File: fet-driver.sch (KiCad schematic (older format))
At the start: 32 parts, among them Q13 AO3401, Q22 AO3401, Q23 AO3401, Q24 AO3401, Q25 AO3401, Q26 AO3401, Q27 AO3401, Q28 AO3401

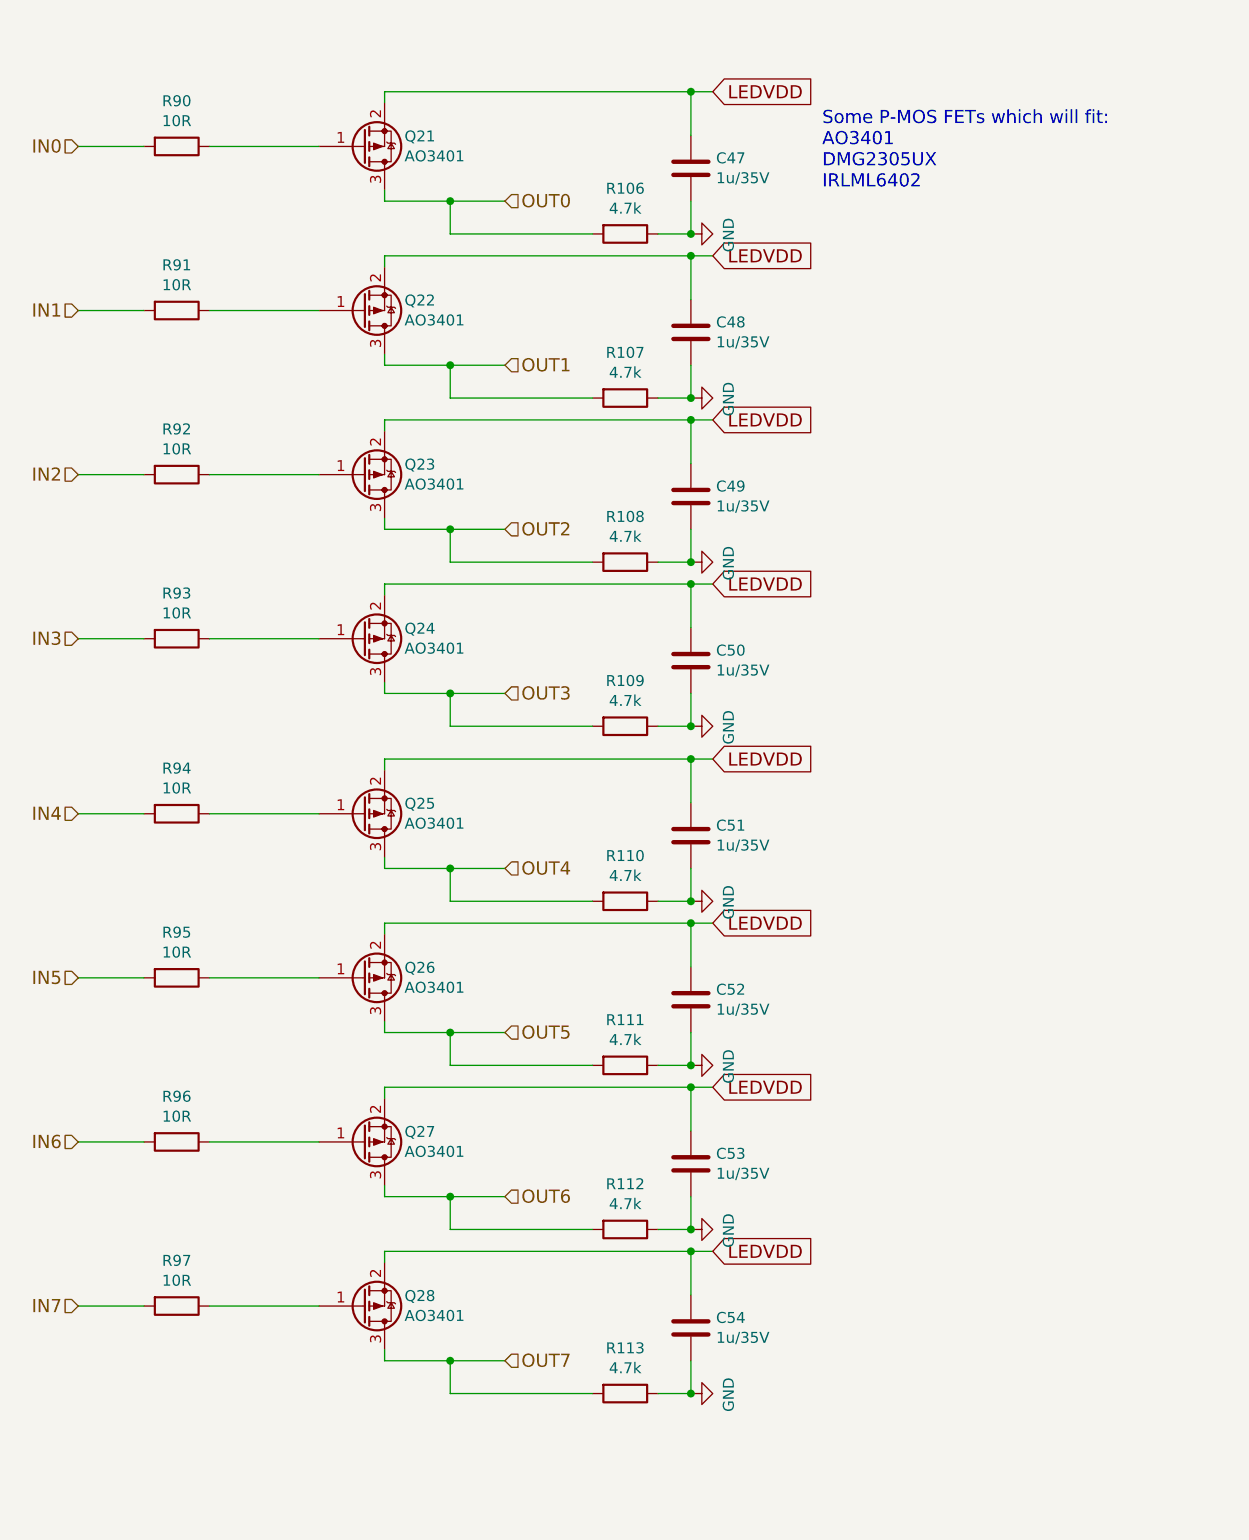
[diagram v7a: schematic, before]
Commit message: Schematics format change due to KiCAD's verup
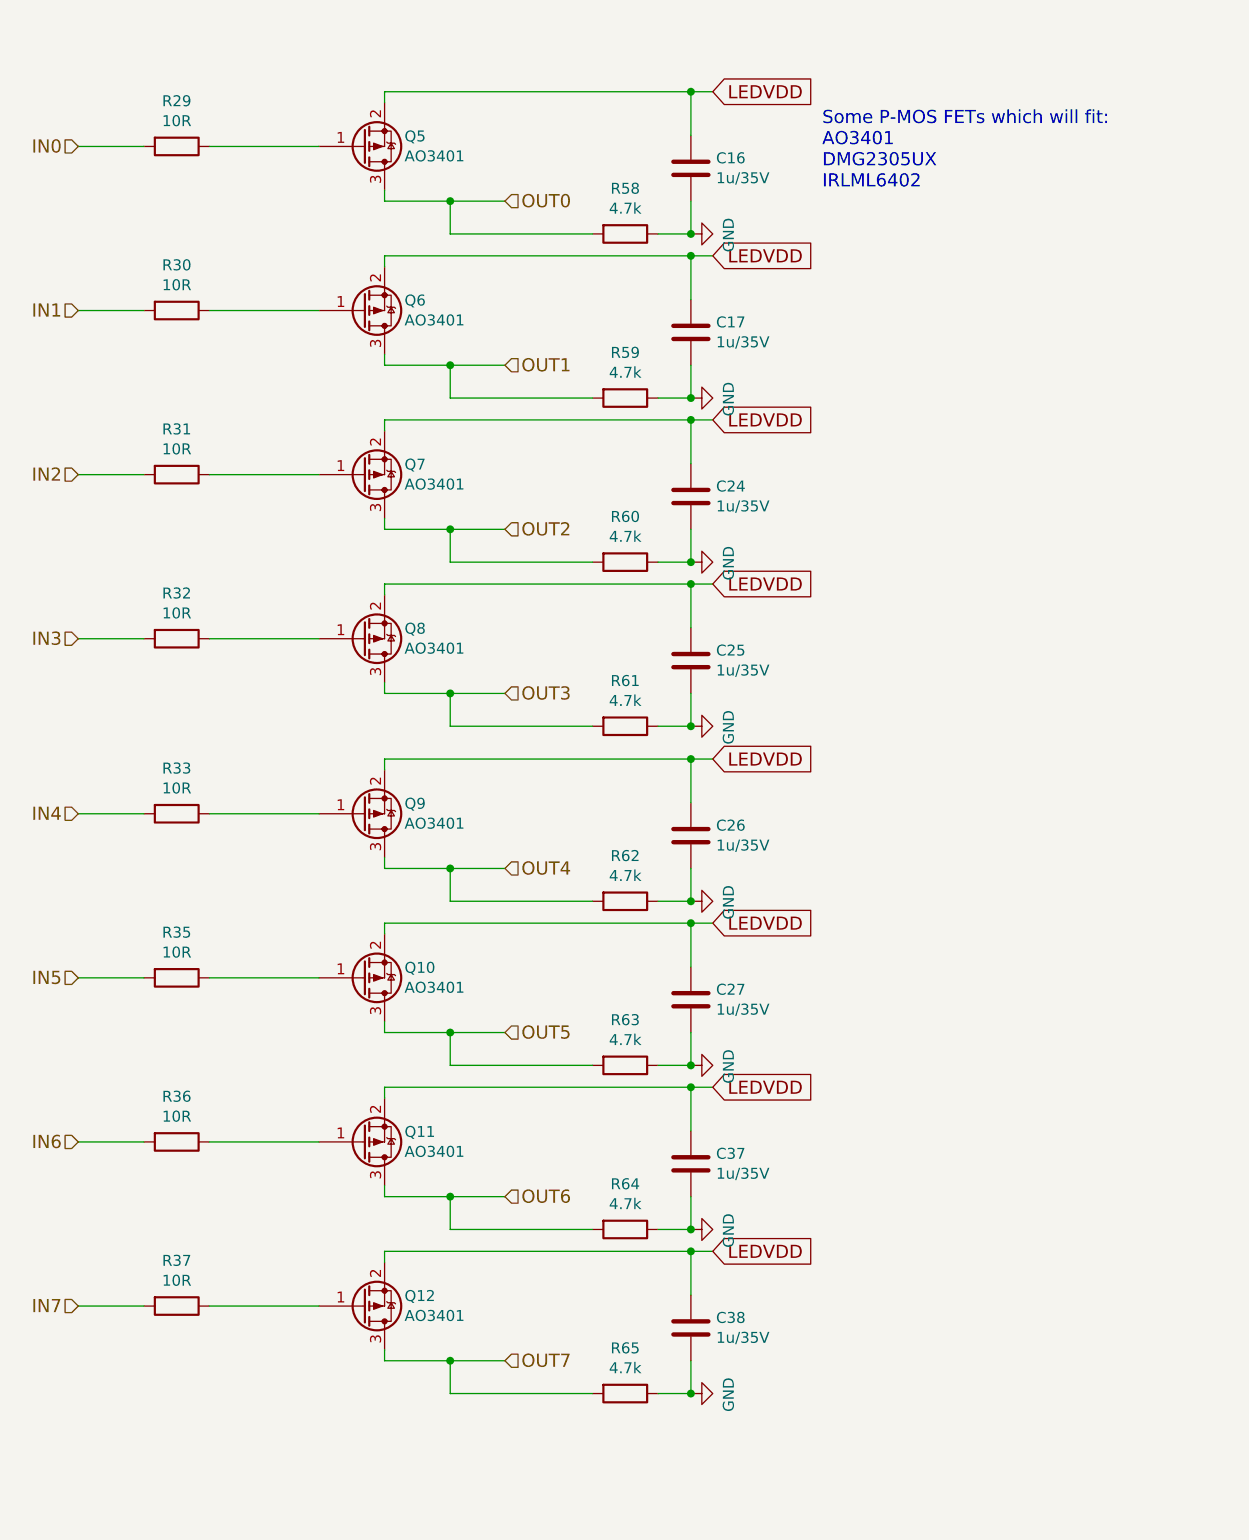
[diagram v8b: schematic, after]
